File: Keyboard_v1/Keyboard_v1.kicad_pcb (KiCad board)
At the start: 2 copper layers, 314.3 x 114.4 mm, 174 parts, among them SW1 SW_Push, U1 ATmega32U4-A, Y1 16MHz

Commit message: all rows and cols connected to MCU
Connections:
- U1 pad 10: unconnected-(U1-PB2-Pad10) -> ROW2
- U1 pad 11: unconnected-(U1-PB3-Pad11) -> ROW3
- U1 pad 18: unconnected-(U1-PD0-Pad18) -> COL13
- U1 pad 19: unconnected-(U1-PD1-Pad19) -> COL12
- U1 pad 20: unconnected-(U1-PD2-Pad20) -> ROW4
- U1 pad 21: unconnected-(U1-PD3-Pad21) -> ROW5
- U1 pad 22: unconnected-(U1-PD5-Pad22) -> COL11
- U1 pad 25: unconnected-(U1-PD4-Pad25) -> COL3
- U1 pad 26: unconnected-(U1-PD6-Pad26) -> COL4
- U1 pad 27: unconnected-(U1-PD7-Pad27) -> COL5
- U1 pad 28: unconnected-(U1-PB4-Pad28) -> COL6
- U1 pad 29: unconnected-(U1-PB5-Pad29) -> COL7
- U1 pad 30: unconnected-(U1-PB6-Pad30) -> COL8
- U1 pad 31: unconnected-(U1-PC6-Pad31) -> COL9
- U1 pad 32: unconnected-(U1-PC7-Pad32) -> COL10
- U1 pad 38: unconnected-(U1-PF5-Pad38) -> COL0
- U1 pad 39: unconnected-(U1-PF4-Pad39) -> COL1
- U1 pad 40: unconnected-(U1-PF1-Pad40) -> COL2
- U1 pad 8: unconnected-(U1-PB0-Pad8) -> ROW0
- U1 pad 9: unconnected-(U1-PB1-Pad9) -> ROW1
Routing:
- net COL9: track 0.00 -> 487.3 mm, vias 0 -> 4
- net COL5: track 0.00 -> 484.2 mm, vias 0 -> 6
- net COL7: track 0.00 -> 478.1 mm, vias 0 -> 4
- net COL6: track 0.00 -> 473.9 mm, vias 0 -> 4
- net COL8: track 0.00 -> 466.4 mm, vias 0 -> 4
- net COL4: track 0.00 -> 461.2 mm, vias 0 -> 6
- net COL3: track 0.00 -> 459.7 mm, vias 0 -> 6
- net COL10: track 0.00 -> 444.6 mm, vias 0 -> 2
- net COL0: track 0.00 -> 426.4 mm, vias 0 -> 4
- net COL1: track 0.00 -> 416.7 mm, vias 0 -> 4
- net COL2: track 0.00 -> 405.0 mm, vias 0 -> 4
- net COL11: track 0.00 -> 288.0 mm, vias 0 -> 2
- net COL12: track 0.00 -> 240.1 mm, vias 0 -> 2
- net COL13: track 0.00 -> 126.2 mm, vias 0 -> 2
- net ROW5: track 321.0 -> 411.5 mm, vias 0 -> 2
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
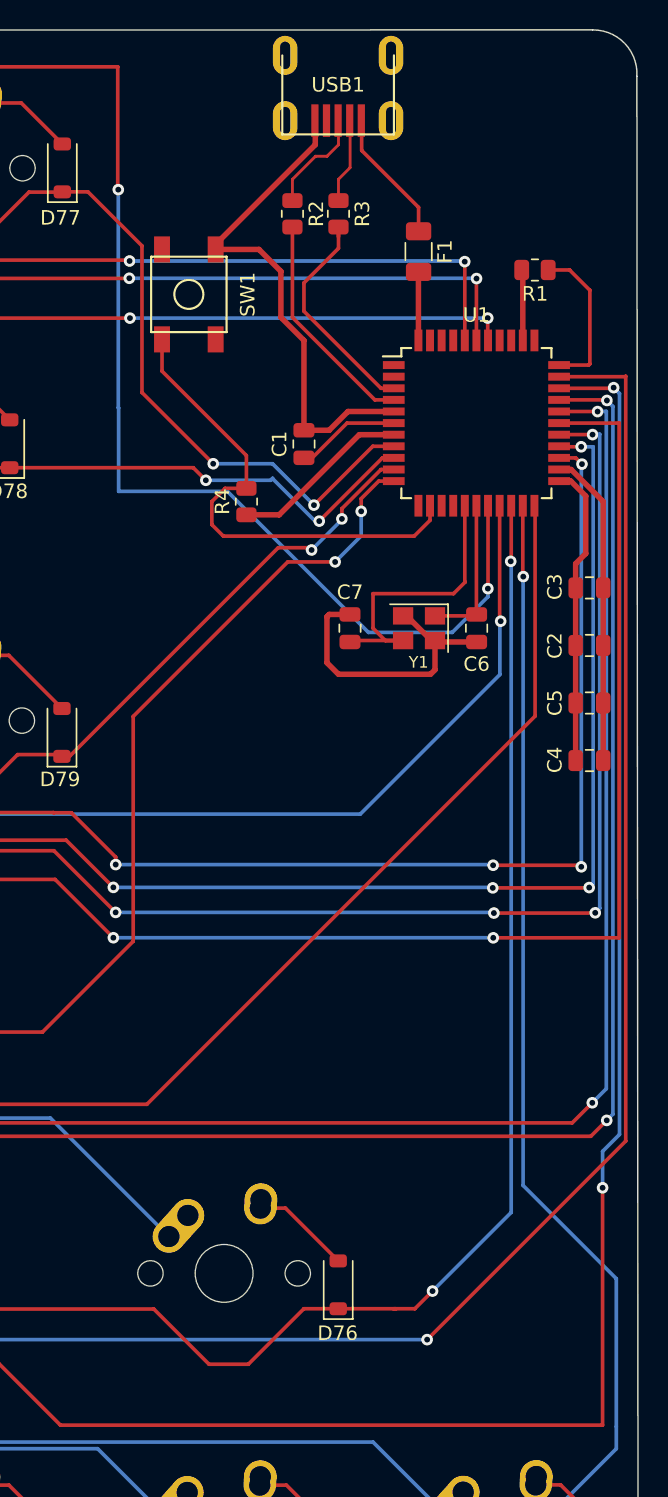
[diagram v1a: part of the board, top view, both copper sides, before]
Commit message: add ground fills
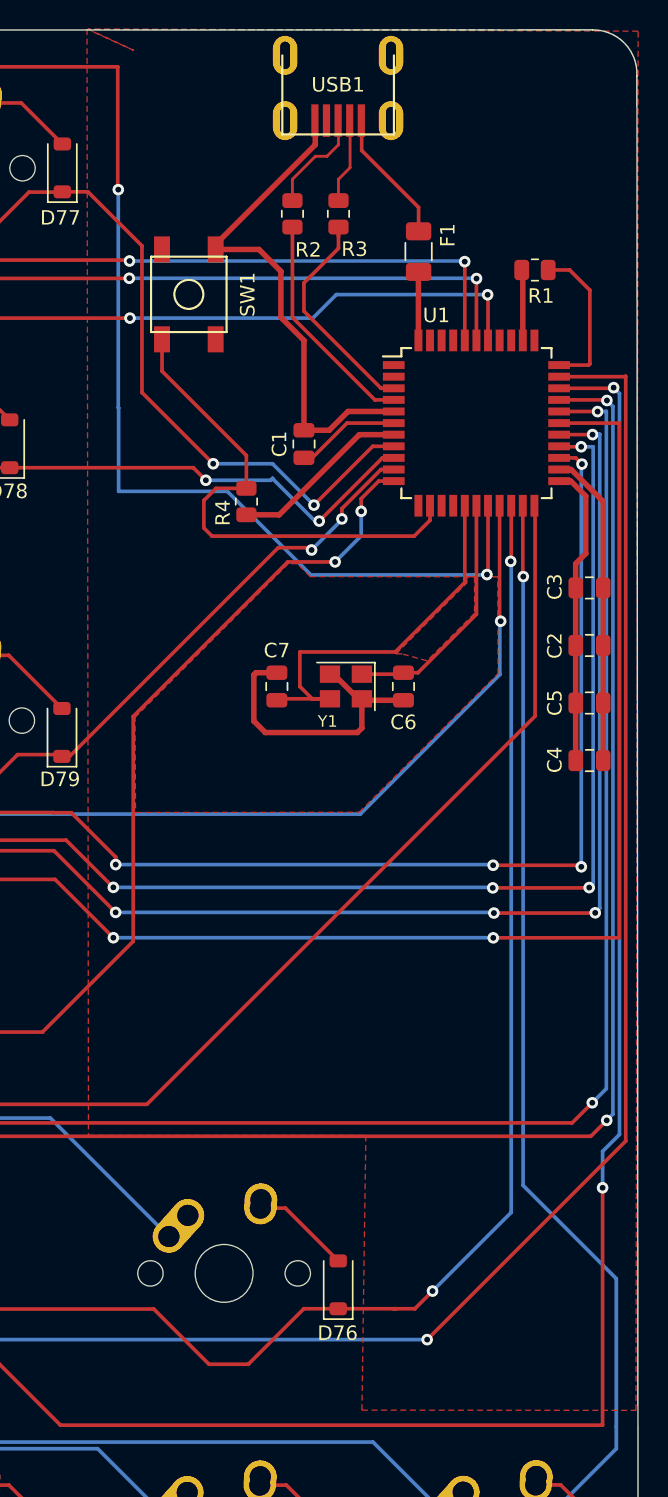
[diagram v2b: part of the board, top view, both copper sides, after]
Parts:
- moved C6 6.45 mm to (409.3, 196.1)
- moved C7 6.45 mm to (400.6, 196.1)
- moved Y1 6.45 mm to (405.3, 196.1)
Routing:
- net Net-(U1-XTAL2): track 20.5 -> 27.2 mm
- net Net-(U1-XTAL1): track 10.4 -> 17.1 mm
- net COL13: track 126.2 -> 122.0 mm
- net COL0: track 426.4 -> 428.7 mm
- net Net-(U1-~{RESET}): track 33.9 -> 35.1 mm
- added copper zone on F.Cu, net GND

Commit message: key matrix done. placing pcb now
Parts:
- moved USB1 0.14 mm to (404.8, 152.4)
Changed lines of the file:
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@@
   )
   (footprint "random-keyboard-parts:Molex-0548190589" (layer "F.Cu")
-    (at 404.786915 152.586164 -90)
+    (at 404.782832 152.441902 -90)
     (property "Sheetfile" "Keyboard_v1.kicad_sch")
     (property "Sheetname" "")
@@
   (segment (start 261.225255 242.169184) (end 264.382598 239.011841) (width 0.254) (layer "F.Cu") (net 102))
   (segment (start 184.265037 242.169185) (end 187.382913 239.051309) (width 0.254) (layer "F.Cu") (net 102))
-  (segment (start 410.079316 239.016899) (end 411.298069 237.798146) (width 0.254) (layer "F.Cu") (net 102))
   (segment (start 157.300959 239.010708) (end 161.272991 242.98274) (width 0.254) (layer "F.Cu") (net 102))
   (segment (start 176.292748 238.972376) (end 179.489557 242.169185) (width 0.254) (layer "F.Cu") (net 102))
@@
   (segment (start 252.540295 239.049039) (end 255.66044 242.169184) (width 0.254) (layer "F.Cu") (net 102))
   (segment (start 214.336453 239.049039) (end 217.417132 242.129718) (width 0.254) (layer "F.Cu") (net 102))
-  (segment (start 408.763083 239.016899) (end 408.767057 239.020873) (width 0.254) (layer "F.Cu") (net 102))
   (segment (start 199.222947 242.169185) (end 203.248558 242.169185) (width 0.254) (layer "F.Cu") (net 102))
   (segment (start 222.942481 242.129718) (end 226.13929 238.932909) (width 0.254) (layer "F.Cu") (net 102))
@@
   (segment (start 304.792684 239.010708) (end 309.646635 239.010708) (width 0.254) (layer "F.Cu") (net 102))
   (segment (start 206.445367 238.972376) (end 209.423772 238.972376) (width 0.254) (layer "F.Cu") (net 102))
-  (segment (start 408.619409 239.016899) (end 410.079316 239.016899) (width 0.254) (layer "F.Cu") (net 102))
   (segment (start 171.298609 239.072635) (end 171.398868 238.972376) (width 0.254) (layer "F.Cu") (net 102))
   (segment (start 398.597688 242.842547) (end 402.423336 239.016899) (width 0.254) (layer "F.Cu") (net 102))
@@
   (segment (start 416.689674 187.478921) (end 416.725 187.443595) (width 0.254) (layer "F.Cu") (net 102))
   (segment (start 342.869224 239.035735) (end 360.197103 239.035735) (width 0.254) (layer "F.Cu") (net 102))
-  (segment (start 408.619409 239.016899) (end 408.763083 239.016899) (width 0.254) (layer "F.Cu") (net 102))
+  (segment (start 410.079316 239.016899) (end 411.298069 237.798146) (width 0.254) (layer "F.Cu") (net 102))
   (segment (start 302.420857 238.978189) (end 304.760165 238.978189) (width 0.254) (layer "F.Cu") (net 102))
   (segment (start 169.015001 239.072635) (end 171.298609 239.072635) (width 0.254) (layer "F.Cu") (net 102))
   (segment (start 171.398868 238.972376) (end 176.292748 238.972376) (width 0.254) (layer "F.Cu") (net 102))
   (segment (start 375.016096 239.010708) (end 375.041123 239.035735) (width 0.254) (layer "F.Cu") (net 102))
+  (segment (start 404.795302 239.016899) (end 410.079316 239.016899) (width 0.254) (layer "F.Cu") (net 102))
   (segment (start 374.983577 238.978189) (end 375.016096 239.010708) (width 0.254) (layer "F.Cu") (net 102))
   (segment (start 242.241736 242.090251) (end 245.282948 239.049039) (width 0.254) (layer "F.Cu") (net 102))
-  (segment (start 404.795302 239.016899) (end 408.619409 239.016899) (width 0.254) (layer "F.Cu") (net 102))
   (segment (start 375.041123 239.035735) (end 392.077622 239.035735) (width 0.254) (layer "F.Cu") (net 102))
   (segment (start 328.713594 238.972376) (end 331.941986 242.200768) (width 0.254) (layer "F.Cu") (net 102))
@@
   (via (at 415.09673 169.093108) (size 0.8) (drill 0.4) (layers "F.Cu" "B.Cu") (net 104))
   (segment (start 124.774188 230.057188) (end 128.778 234.061) (width 0.254) (layer "B.Cu") (net 104))
-  (segment (start 118.682038 157.82875) (end 115.52218 160.988608) (width 0.254) (layer "B.Cu") (net 104))
-  (segment (start 121.72125 157.82875) (end 118.682038 157.82875) (width 0.254) (layer "B.Cu") (net 104))
   (segment (start 415.084156 169.080534) (end 415.09673 169.093108) (width 0.254) (layer "B.Cu") (net 104))
   (segment (start 121.72125 157.82875) (end 121.471189 158.078811) (width 0.254) (layer "B.Cu") (net 104))
@@
   (segment (start 121.72125 195.92875) (end 121.72125 197.205308) (width 0.254) (layer "B.Cu") (net 104))
   (segment (start 122.359471 213.244188) (end 124.085035 214.969752) (width 0.254) (layer "B.Cu") (net 104))
+  (segment (start 118.682038 157.82875) (end 121.72125 157.82875) (width 0.254) (layer "B.Cu") (net 104))
   (segment (start 124.085035 216.247492) (end 124.774188 216.936645) (width 0.254) (layer "B.Cu") (net 104))
   (segment (start 124.085035 214.969752) (end 124.085035 216.247492) (width 0.254) (layer "B.Cu") (net 104))
@@
   (segment (start 116.95875 176.87875) (end 116.95875 177.991668) (width 0.254) (layer "B.Cu") (net 104))
   (segment (start 117.711624 191.919124) (end 121.72125 195.92875) (width 0.254) (layer "B.Cu") (net 104))
+  (segment (start 115.52218 160.988608) (end 118.682038 157.82875) (width 0.254) (layer "B.Cu") (net 104))
   (segment (start 146.84375 156.36875) (end 149.902635 153.309865) (width 0.254) (layer "F.Cu") (net 105))
   (segment (start 390.377557 167.966704) (end 390.388024 167.956237) (width 0.254) (layer "F.Cu") (net 105))
